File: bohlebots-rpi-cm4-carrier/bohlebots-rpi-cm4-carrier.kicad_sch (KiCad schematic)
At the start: 24 parts, among them J1 SI-46001-F, J2 power_reference, J3 REF_OUT_Conn_02x05, K1 Kicker, T1 Taster_LED, T2 Taster_LED, U1 Compute_Module_4_Connectors, U2 USB_Conn_01x05_Pin, X1 Miromatch

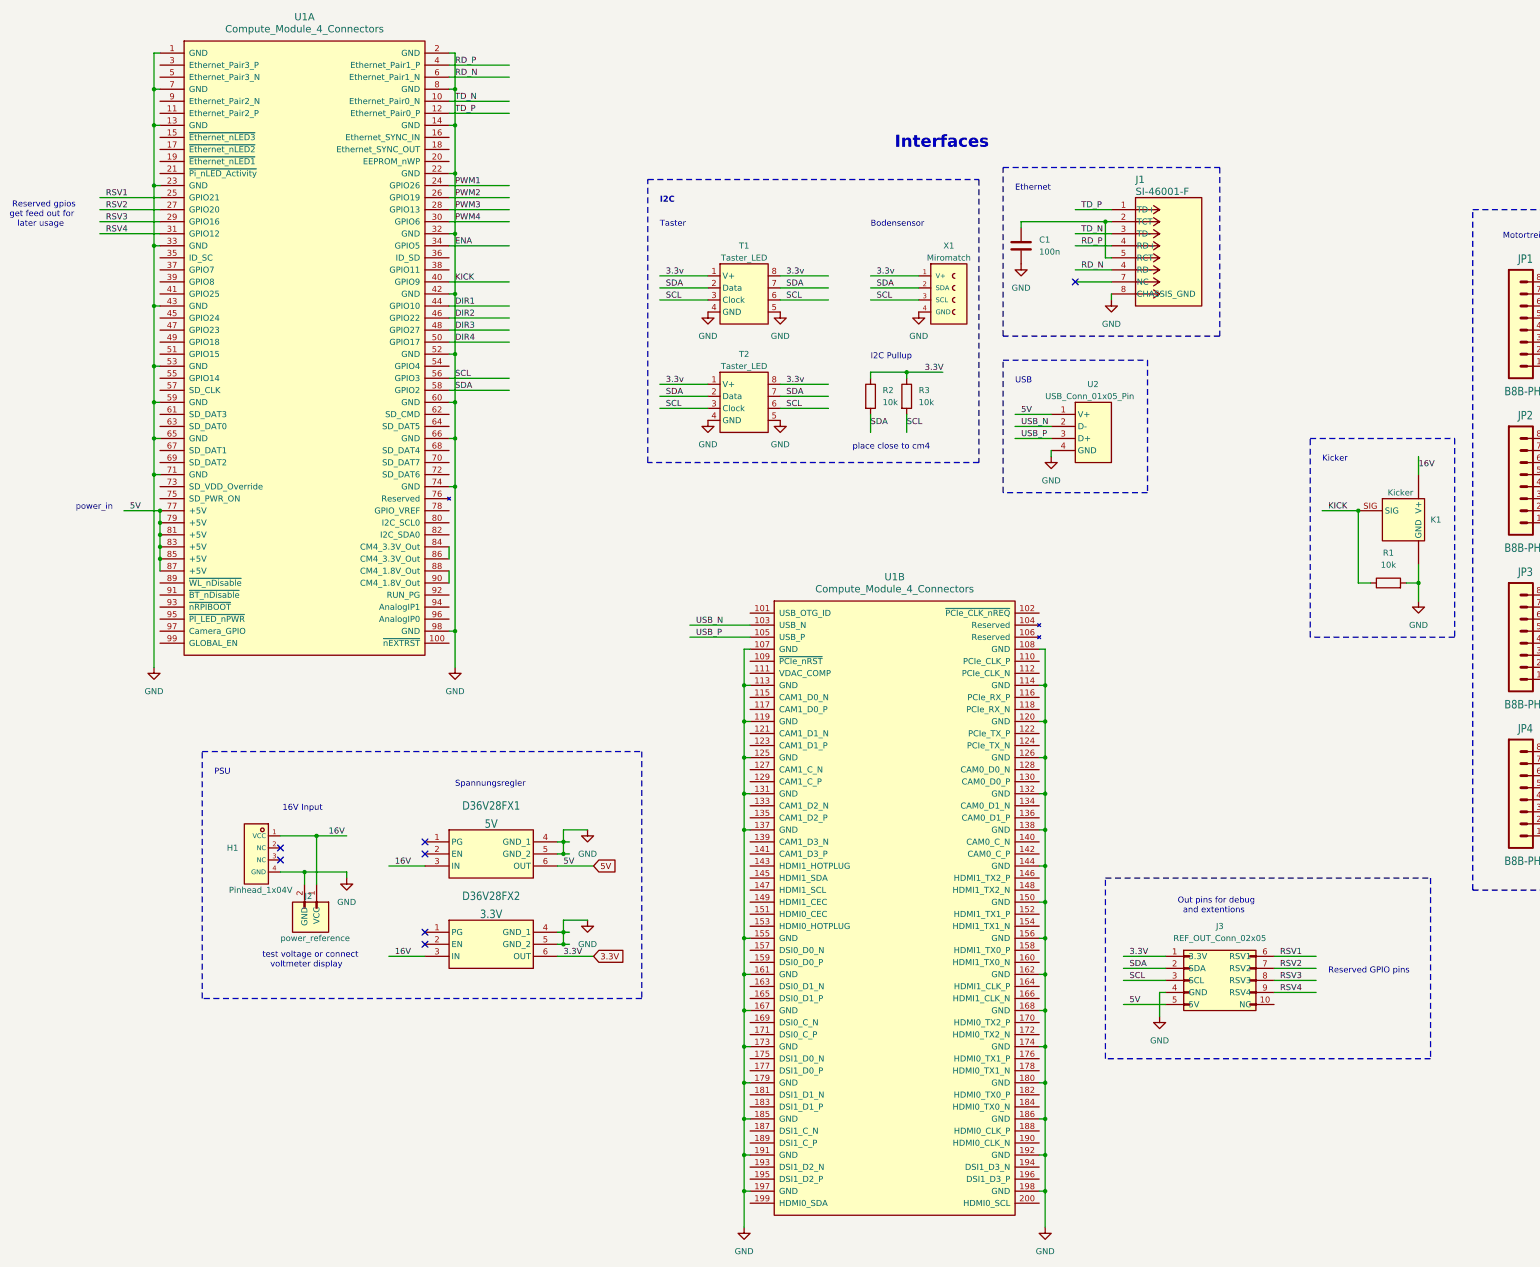
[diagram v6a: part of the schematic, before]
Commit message: Finished Schematic, started pcb.
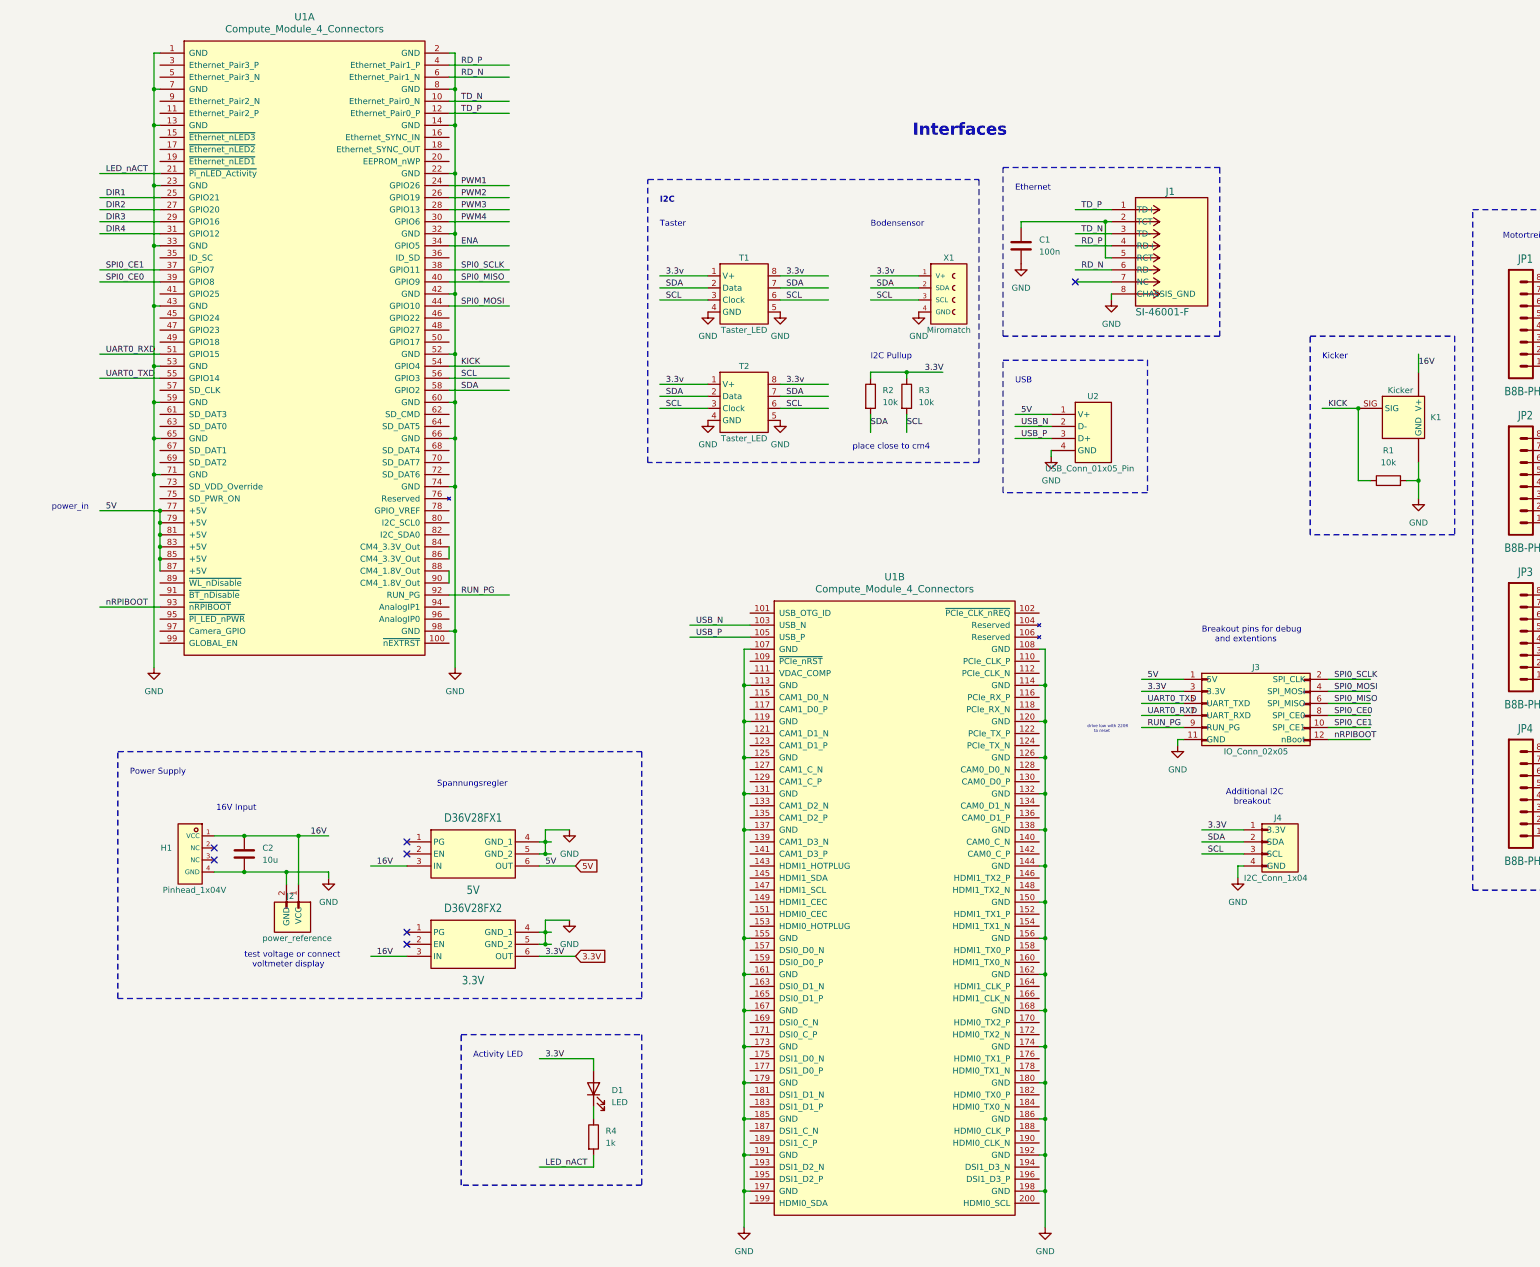
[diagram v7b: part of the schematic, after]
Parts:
- removed J3: REF_OUT_Conn_02x05, Connector_PinHeader_2.54mm:PinHeader_2x05_P2.54mm_Vertical, symbol Connector_Generic:Conn_02x05_Top_Bottom
- added C2: 10u, Capacitor_THT:C_Radial_D5.0mm_H11.0mm_P2.00mm, symbol Device:C
- added D1: LED, LED_THT:LED_D5.0mm_FlatTop, symbol Device:LED
- added J3: IO_Conn_02x05, Connector_PinHeader_2.54mm:PinHeader_2x06_P2.54mm_Vertical, symbol Connector_Generic:Conn_02x05_Odd_Even
- added J4: I2C_Conn_1x04, Connector_PinHeader_2.54mm:PinHeader_1x04_P2.54mm_Vertical, symbol Connector_Generic:Conn_01x04
- added R4: 1k, Resistor_THT:R_Axial_DIN0207_L6.3mm_D2.5mm_P7.62mm_Horizontal, symbol Device:R
- C1: footprint Capacitor_THT:CP_Axial_L10.0mm_D4.5mm_P15.00mm_Horizontal -> Capacitor_THT:C_Radial_D5.0mm_H11.0mm_P2.00mm
- R1: footprint Resistor_THT:R_Array_SIP4 -> Resistor_THT:R_Axial_DIN0207_L6.3mm_D2.5mm_P7.62mm_Horizontal
- R2, R3: footprint (none) -> Resistor_THT:R_Axial_DIN0207_L6.3mm_D2.5mm_P7.62mm_Horizontal
- U2: footprint Connector_PinHeader_2.54mm:PinHeader_1x05_P2.54mm_Vertical -> Connector_PinHeader_2.54mm:PinHeader_1x04_P2.54mm_Vertical
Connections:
- net 16V: now also C2.1
- net 3.3V: now also D1.2 (A), J3.3 (3.3V), J4.1 (3.3V)
- net 5V: now also J3.1 (5V)
- net GND: now also C2.2, J3.11 (GND), J4.4 (GND); no longer ESCON1.P15 (D3), ESCON1.P16 (D2), ESCON1.P17 (D1), ESCON2.P15 (D3), ESCON2.P16 (D2), ESCON2.P17 (D1), ESCON3.P15 (D3), ESCON3.P16 (D2), ESCON3.P17 (D1), ESCON4.P15 (D3), ESCON4.P16 (D2), ESCON4.P17 (D1), J1.1 (TD+), J1.3 (TD-), J1.4 (RD-), K1.SIG, R1.1, R2.2, R3.2, T1.2 (Data), T1.3 (Clock), T1.6, T1.7, T2.2 (Data), T2.3 (Clock), T2.6, T2.7, U1.10 (Ethernet_Pair0_N), U1.12 (Ethernet_Pair0_P), U1.24 (GPIO26), U1.26 (GPIO19), U1.28 (GPIO13), U1.30 (GPIO6), U1.34 (GPIO5), U1.4 (Ethernet_Pair1_P), U1.40 (GPIO9), U1.44 (GPIO10), U1.46 (GPIO22), U1.48 (GPIO27), U1.50 (GPIO17), U1.56 (GPIO3), U1.58 (GPIO2), U1.6 (Ethernet_Pair1_N), X1.2 (SDA), X1.3 (SCL)
- net LED_nACT: now reaches U1.21 (~{Pi_nLED_Activity})
- net LED_nACT: now also R4.2
- net SPI0_CE1: now reaches U1.37 (GPIO7)
- net SPI0_CE1: now also J3.10 (SPI_CE1)
- net SPI0_SCLK: now reaches U1.38 (GPIO11)
- net SPI0_SCLK: now also J3.2 (SPI_CLK)
- net SPI0_CE0: now reaches U1.39 (GPIO8)
- net SPI0_CE0: now also J3.8 (SPI_CE0)
- net UART0_RXD: now reaches U1.51 (GPIO15)
- net UART0_RXD: now also J3.7 (UART_RXD)
- net KICK: now reaches U1.54 (GPIO4)
- net KICK: now also K1.SIG, R1.1
- net UART0_TXD: now reaches U1.55 (GPIO14)
- net UART0_TXD: now also J3.5 (UART_TXD)
- net RUN_PG: now reaches U1.92 (RUN_PG)
- net RUN_PG: now also J3.9 (RUN_PG)
- net nRPIBOOT: now reaches U1.93 (~{nRPIBOOT})
- net nRPIBOOT: now also J3.12 (nBoot)
- net RSV1 renamed DIR1
- net DIR1: now also ESCON1.P15 (D3), ESCON2.P15 (D3), ESCON3.P15 (D3), ESCON4.P15 (D3)
- net RSV2 renamed DIR2
- net RSV3 renamed DIR3
- net RSV4 renamed DIR4
- new net: D1.1 (K), R4.1
- new net ENA: ESCON1.P16 (D2), ESCON2.P16 (D2), ESCON3.P16 (D2), ESCON4.P16 (D2), U1.34 (GPIO5)
- new net PWM1: ESCON1.P17 (D1), ESCON2.P17 (D1), ESCON3.P17 (D1), ESCON4.P17 (D1), U1.24 (GPIO26)
- new net PWM2: U1.26 (GPIO19)
- new net PWM3: U1.28 (GPIO13)
- new net PWM4: U1.30 (GPIO6)
- new net RD_N: J1.6 (RD-), U1.6 (Ethernet_Pair1_N)
- new net RD_P: J1.4 (RD+), U1.4 (Ethernet_Pair1_P)
- new net SCL: J4.3 (SCL), R3.2, T1.3 (Clock), T1.6, T2.3 (Clock), T2.6, U1.56 (GPIO3), X1.3 (SCL)
- new net SDA: J4.2 (SDA), R2.2, T1.2 (Data), T1.7, T2.2 (Data), T2.7, U1.58 (GPIO2), X1.2 (SDA)
- new net SPI0_MISO: J3.6 (SPI_MISO), U1.40 (GPIO9)
- new net SPI0_MOSI: J3.4 (SPI_MOSI), U1.44 (GPIO10)
- new net TD_N: J1.3 (TD-), U1.10 (Ethernet_Pair0_N)
- new net TD_P: J1.1 (TD+), U1.12 (Ethernet_Pair0_P)
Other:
- note added: "Activity LED"
- note added: "Additional I2C breakout"
- note added: "Breakout pins for debug and extentions"
- note added: "Power Supply"
- note added: "drive low with 220R to reset"
- note removed: "Out pins for debug and extentions"
- note removed: "PSU"
- note removed: "Reserved GPIO pins"
- note removed: "Reserved gpios get feed out for later usage"
- title: (none) -> Compute Module 4 Carrier - Bohlebots BigBrother
- moved on the sheet: D36V28FX1, D36V28FX2, H1, J2, K1, R1
